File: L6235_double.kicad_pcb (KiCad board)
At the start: 2 copper layers, 110 x 55 mm, 68 parts, among them J1 conn_2x16, J2 CONN_01X04, P1 CONN_01X03, P2 CONN_01X03, P4 CONN_01X02, P5 CONN_01X02, P7 CONN_01X02, P8 CONN_01X02, U1 L6235N, U2 L6235N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

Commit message: cosmetic changes
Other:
- board text added: "CAN-ID :"

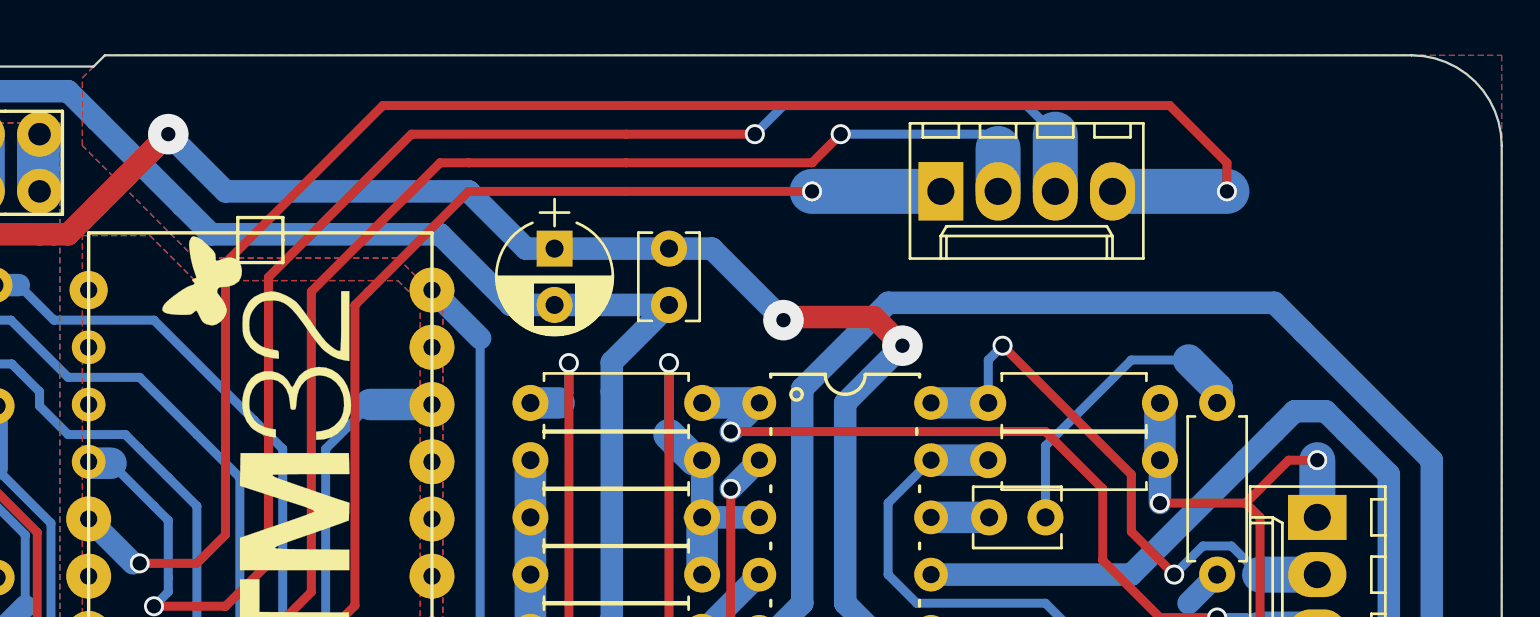
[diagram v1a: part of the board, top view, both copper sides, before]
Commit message: changed encoder connectors
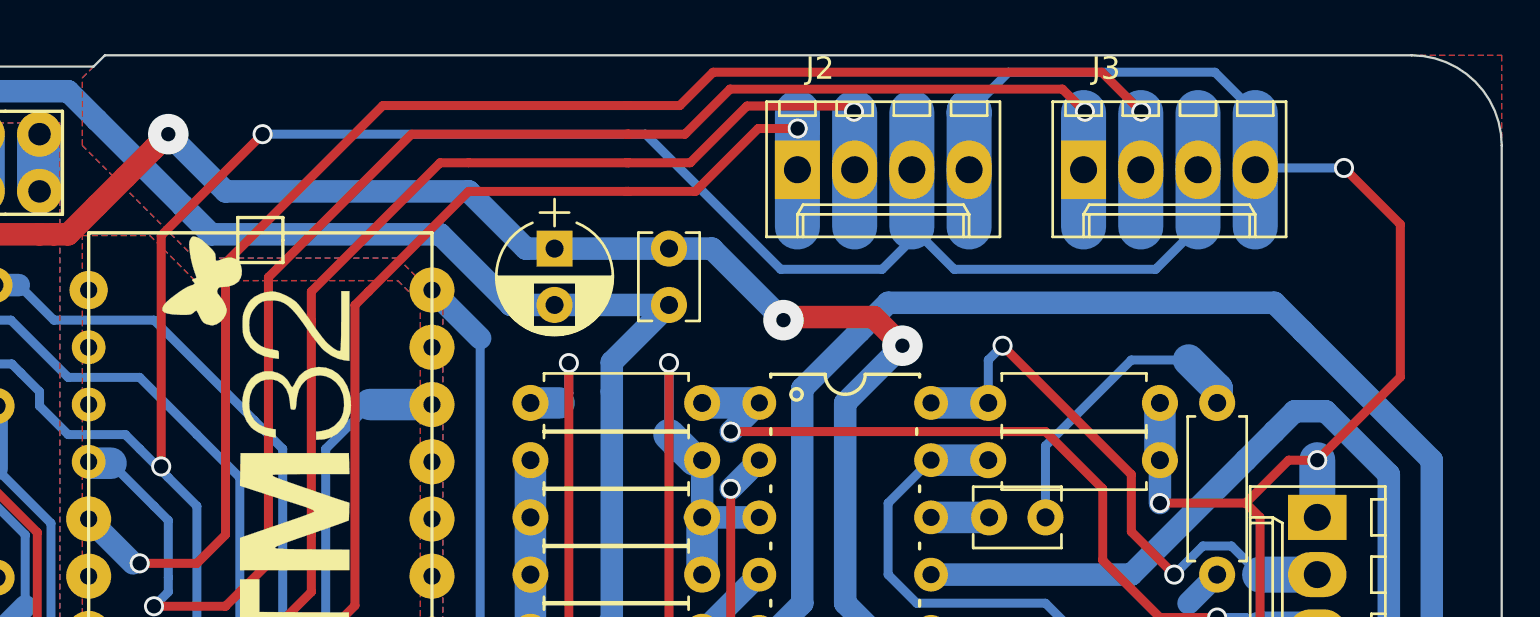
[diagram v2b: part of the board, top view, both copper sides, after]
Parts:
- added J3: Conn_01x04, Connectors_Molex:Molex_KK-6410-04_04x2.54mm_Straight, F.Cu at (122.4, 52.1)
- J2: value CONN_01X04 -> Conn_01x04
- U3: value Nucleo -> Nano
- moved J2 6.44 mm to (109.7, 52.1)
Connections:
- J2 pad 3: /ENC_R_A -> /GNDL
- J2 pad 4: /ENC_R_B -> /+5L
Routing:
- net /GNDL: track 101.7 -> 178.1 mm, vias 2 -> 4
- net /+5L: track 278.3 -> 322.2 mm, vias 11 -> 12
- net /ENC_R_B: track 74.2 -> 69.6 mm
- net /ENC_R_A: track 68.4 -> 72.6 mm
- net /ENC_L_B: track 60.2 -> 57.5 mm
